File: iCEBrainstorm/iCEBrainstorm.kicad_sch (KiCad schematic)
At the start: 1 part

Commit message: commit from within kicad
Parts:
- added C1, C2, C3, C4, C5: 100nF, PCM_JLCPCB:C_0603, symbol PCM_JLCPCB-Capacitors:0603,100nF
- added C6: 4.7uF, PCM_JLCPCB:C_0805, symbol PCM_JLCPCB-Capacitors:0805,4.7uF
- added C7, C8: 1uF, PCM_JLCPCB:C_0603, symbol PCM_JLCPCB-Capacitors:0603,1uF
- added C9: 10nF, PCM_JLCPCB:C_0603, symbol PCM_JLCPCB-Capacitors:0603,10nF
- added FB1: ~, PCM_JLCPCB:FB_0805, symbol PCM_JLCPCB-Inductors:Ferrite,0805,(2)
- added SW1: BOOT MODE, symbol Switch:SW_SPDT
- added SW2: Tactile Button, 160gf, PCM_JLCPCB:SW_TS-1088-AR02016, symbol PCM_JLCPCB-Connectors_Buttons:Tactile Button, 160gf, 12V, 50mA, 4.0mm
- added U1: STM32F103C8T6, PCM_JLCPCB:LQFP-48_7x7mm_P0.5mm, symbol PCM_JLCPCB-MCUs:STM32F103C8T6
- added U2: CH32V003F4U6, PCM_JLCPCB:QFN-20-1EP_3x3mm_P0.4mm_EP1.65x1.65mm, symbol PCM_JLCPCB-Extended:MCU, CH32V003F4U6
- added U3: ICE40UP5K-SG48ITR, Package_DFN_QFN:QFN-48-1EP_7x7mm_P0.5mm_EP5.6x5.6mm, symbol FPGA_Lattice:ICE40UP5K-SG48ITR
- added X1: X322516MLB4SI, PCM_JLCPCB:OSC-SMD_4P-L3.2-W2.5-BL, symbol PCM_JLCPCB-Crystals:Crystal, 16MHz, 9pF
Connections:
- net at R1.1: now also SW1.2 (B)
- net at R1.2: now also U1.44 (BOOT0)
- new net: U3.30 (VCC), U3.5 (VCC)
- new net: U2.21 (VSS), U2.4 (VSS)
- new net +3.3VA: C8.1, C9.1, FB1.1, U1.9 (VDDA)
- new net +3V3: C2.1, C3.1, C4.1, C5.1, C6.1, C7.1, FB1.2, SW1.1 (A), U1.1 (VBAT), U1.24 (VDD), U1.36 (VDD), U1.48 (VDD)
- new net GND: C1.2, C2.2, C3.2, C4.2, C5.2, C6.2, C7.2, C8.2, C9.2, SW1.3 (C), SW2.2 (B), U1.23 (VSS), U1.35 (VSS), U1.47 (VSS), U1.8 (VSSA)
- new net NRST: C1.1, SW2.1 (A), U1.7 (NRST)
- new net XMIN: U1.6 (PD1), X1.3 (OSC)
- new net XPLUS: U1.5 (PD0), X1.1 (OSC)

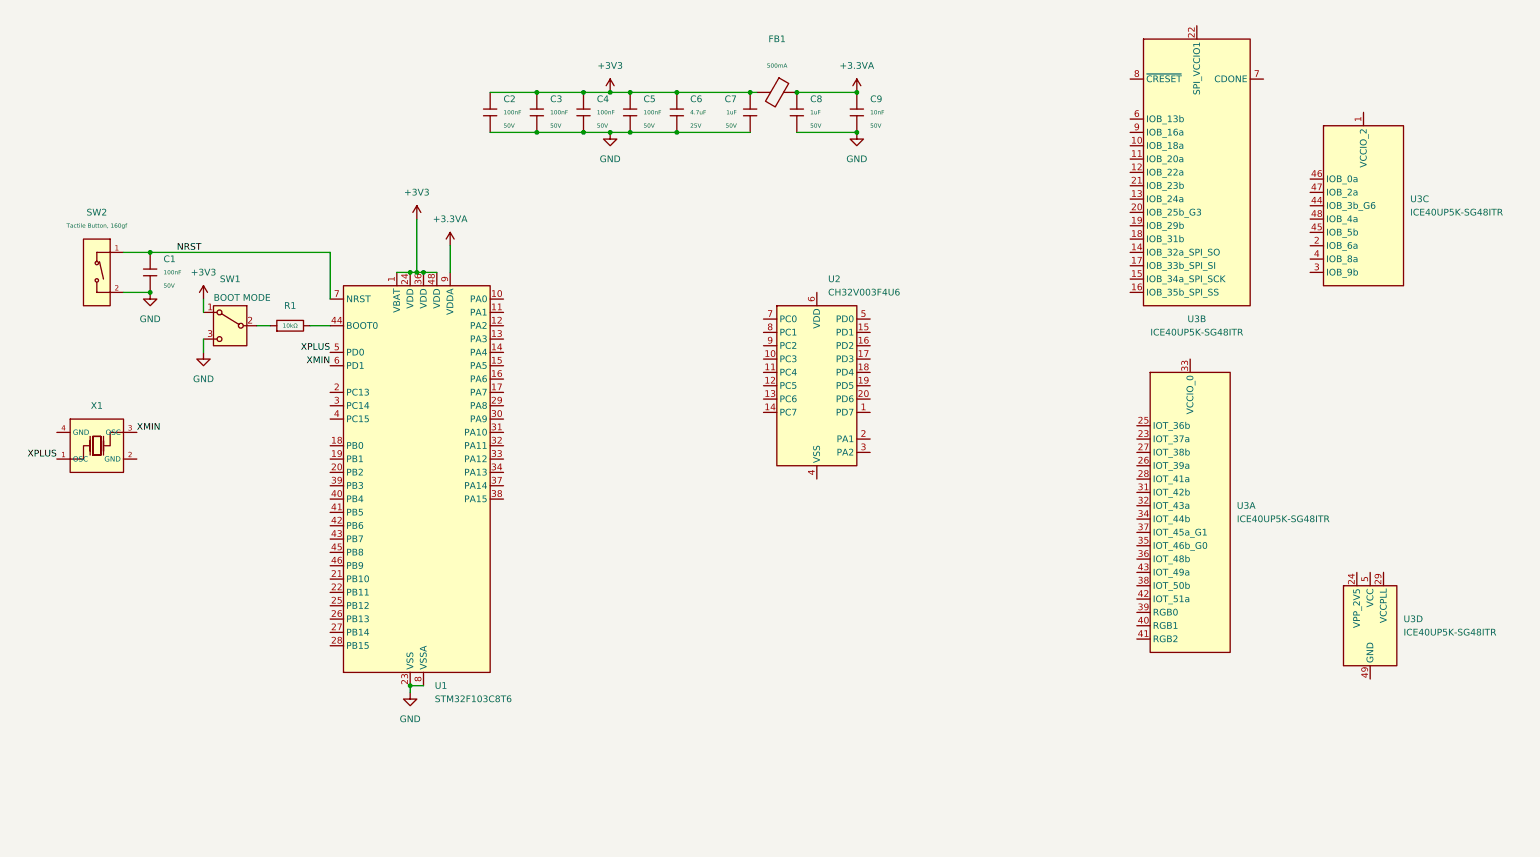
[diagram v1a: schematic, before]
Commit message: added some things to schematic
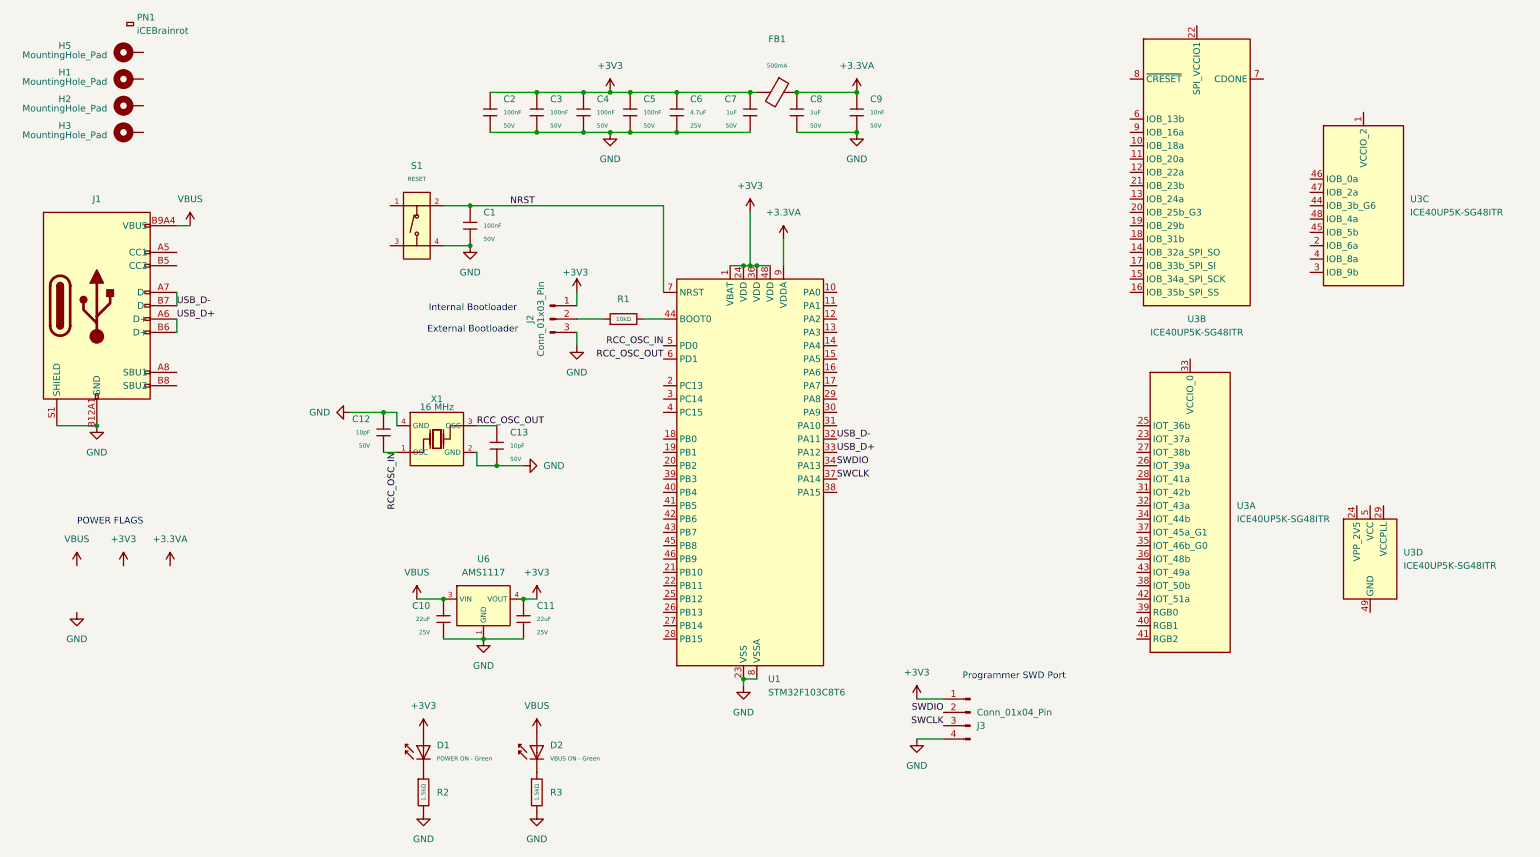
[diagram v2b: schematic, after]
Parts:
- removed SW1: BOOT MODE, symbol Switch:SW_SPDT
- removed SW2: Tactile Button, 160gf, PCM_JLCPCB:SW_TS-1088-AR02016, symbol PCM_JLCPCB-Connectors_Buttons:Tactile Button, 160gf, 12V, 50mA, 4.0mm
- removed U2: CH32V003F4U6, PCM_JLCPCB:QFN-20-1EP_3x3mm_P0.4mm_EP1.65x1.65mm, symbol PCM_JLCPCB-Extended:MCU, CH32V003F4U6
- added C10, C11: 22uF, PCM_JLCPCB:C_0805, symbol PCM_JLCPCB-Capacitors:0805,22uF
- added C12, C13: 10pF, PCM_JLCPCB:C_0603, symbol PCM_JLCPCB-Capacitors:0603,10pF
- added D1: POWER ON - Green, PCM_JLCPCB:D_0805, symbol PCM_JLCPCB-Diodes:LED,0805,Green
- added D2: VBUS ON - Green, PCM_JLCPCB:D_0805, symbol PCM_JLCPCB-Diodes:LED,0805,Green
- added H1, H2, H3: MountingHole_Pad, MountingHole:MountingHole_2.7mm_Pad, symbol Mechanical:MountingHole_Pad
- added H5: MountingHole_Pad, MountingHole:MountingHole_3.2mm_M3_DIN965_Pad, symbol Mechanical:MountingHole_Pad
- added J1: Connector, USB-TYPE-C-16P, PCM_JLCPCB:TYPE-C-SMD_HX-TYPE-C-16PIN, symbol PCM_JLCPCB-Extended:Connector, USB-TYPE-C-16P
- added J2: Conn_01x03_Pin, Connector_PinHeader_2.00mm:PinHeader_1x03_P2.00mm_Vertical, symbol Connector:Conn_01x03_Pin
- added J3: Conn_01x04_Pin, Connector_PinHeader_2.00mm:PinHeader_1x04_P2.00mm_Vertical, symbol Connector:Conn_01x04_Pin
- added PN1: iCEBrainrot, PCM_JLCPCB:Part_Num_JLCPCB, symbol PCM_JLCPCB-Manufacturing:Part Number, PCM_JLCPCB, 0.8x0.15mm
- added R2, R3: 1.5kΩ, PCM_JLCPCB:R_0603, symbol PCM_JLCPCB-Resistors:0603,1.5kΩ
- added S1: RESET, PCM_JLCPCB:SW-SMD_4P-L5.1-W5.1-P3.70-LS6.5-TL-2, symbol PCM_JLCPCB-Connectors_Buttons:Tactile Button, 160gf, 12V, 50mA, 5.1mm
- added U6: AMS1117, PCM_JLCPCB:SOT-223-3_L6.5-W3.4-P2.30-LS7.0-BR, symbol PCM_JLCPCB-Power:LDO, 3.3V, 1A
- X1: value X322516MLB4SI -> 16 MHz
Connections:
- net +3V3: now also C11.2, D1.2, J2.1 (Pin_1), J3.1 (Pin_1), U6.2 (VOUT), U6.4 (VOUT)
- net GND: now also X1.2 (GND), X1.4 (GND), C10.1, C11.1, C12.1, C13.2, J1.A12B1 (GND), J1.B12A1 (GND), J1.S1 (SHIELD), J2.3 (Pin_3), J3.4 (Pin_4), R2.2, R3.2, S1.4 (D), U6.1 (GND)
- net NRST: now also S1.2 (B)
- net at R1.1: now also J2.2 (Pin_2)
- net USB_D-: now reaches U1.32 (PA11)
- net USB_D-: now also J1.A7 (D-), J1.B7 (D-)
- net USB_D+: now reaches U1.33 (PA12)
- net USB_D+: now also J1.A6 (D+), J1.B6 (D+)
- net SWDIO: now reaches U1.34 (PA13)
- net SWDIO: now also J3.2 (Pin_2)
- net SWCLK: now reaches U1.37 (PA14)
- net SWCLK: now also J3.3 (Pin_3)
- net XMIN renamed RCC_OSC_OUT
- net RCC_OSC_OUT: now also C13.1
- net XPLUS renamed RCC_OSC_IN
- net RCC_OSC_IN: now also C12.2
- new net: D1.1, R2.1
- new net: D2.1, R3.1
- new net VBUS: C10.2, D2.2, J1.A9B4 (VBUS), J1.B9A4 (VBUS), U6.3 (VIN)
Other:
- note added: "Internal Bootloader External Bootloader"
- note added: "POWER FLAGS"
- note added: "Programmer SWD Port"
- moved on the sheet: C1, R1, U1, U3D, X1

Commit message: did some things
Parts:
- removed H5: MountingHole_Pad, MountingHole:MountingHole_3.2mm_M3_DIN965_Pad, symbol Mechanical:MountingHole_Pad
- removed J2: Conn_01x03_Pin, Connector_PinHeader_2.00mm:PinHeader_1x03_P2.00mm_Vertical, symbol Connector:Conn_01x03_Pin
- removed R1: 10kΩ, PCM_JLCPCB:R_0603, symbol PCM_JLCPCB-Resistors:0603,10kΩ
- removed U1: STM32F103C8T6, PCM_JLCPCB:LQFP-48_7x7mm_P0.5mm, symbol PCM_JLCPCB-MCUs:STM32F103C8T6
- added C14, C16, C18: 4.7uF, PCM_JLCPCB:C_0805, symbol PCM_JLCPCB-Capacitors:0805,4.7uF
- added C15, C17, C19: 100nF, PCM_JLCPCB:C_0603, symbol PCM_JLCPCB-Capacitors:0603,100nF
- added C20, C21: 22uF, PCM_JLCPCB:C_0805, symbol PCM_JLCPCB-Capacitors:0805,22uF
- added H4: MountingHole_Pad, MountingHole:MountingHole_2.7mm_Pad, symbol Mechanical:MountingHole_Pad
- added R1, R6: 15kΩ, PCM_JLCPCB:R_0603, symbol PCM_JLCPCB-Resistors:0603,15kΩ
- added R4, R5: 5.1kΩ, PCM_JLCPCB:R_0603, symbol PCM_JLCPCB-Resistors:0603,5.1kΩ
- added SW1, SW2: SW_DIP_x08, Button_Switch_THT:SW_DIP_SPSTx08_Slide_6.7x21.88mm_W7.62mm_P2.54mm_LowProfile, symbol Switch:SW_DIP_x08
- added U1: AMS1117-1.2, PCM_JLCPCB:SOT-223-3_L6.5-W3.4-P2.30-LS7.0-BR, symbol PCM_JLCPCB-Power:LDO, 3.3V, 1A
- added U2: STM32F412RETx, Package_QFP:LQFP-64_10x10mm_P0.5mm, symbol MCU_ST_STM32F4:STM32F412RETx
- U6: value AMS1117 -> AMS1117-3.3
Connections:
- net +3.3VA: now also U2.13 (VDDA)
- net +3V3: now also U3.1 (VCCIO_2), U3.22 (SPI_VCCIO1), U3.24 (VPP_2V5), U3.33 (VCCIO_0), C14.1, C15.1, C16.1, C17.1, C18.1, C19.1, SW1.15, SW1.16, U2.1 (VBAT), U2.19 (VDD), U2.32 (VDD), U2.48 (VDD), U2.64 (VDD)
- net GND: now also U3.49 (GND), C14.2, C15.2, C16.2, C17.2, C18.2, C19.2, C20.1, C21.1, R1.2, R4.2, R5.2, R6.2, U1.1 (GND), U2.12 (VSSA), U2.18 (VSS), U2.31 (VSS), U2.47 (VSS), U2.63 (VSS)
- net NRST: now also U2.7 (NRST)
- net VBUS: now also C20.2, U1.3 (VIN)
- net VCCPLL: now reaches U3.29 (VCCPLL)
- net +1V2: now reaches U3.30 (VCC), U3.5 (VCC)
- net +1V2: now also C21.2, U1.2 (VOUT), U1.4 (VOUT)
- net at U3.25 (IOT_36b): now also U2.14 (PA0)
- net at J1.A5 (CC1): now also R4.1
- net at J1.B5 (CC2): now also R5.1
- new net BOOT0: R1.1, SW1.1, U2.60 (BOOT0)
- new net BOOT1: R6.1, SW1.2, U2.28 (PB2)
- no-connect marks 0 -> 2
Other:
- note added: "5k1 Resistor like in this Tutorial"
- note added: "SW1 OFF: Custom Boot SW1 ON: STM Bootloader SW2 OFF: System Memory (default) SW2 ON: Embedded SRAM Boot"
- note added: "note: this is not 100% correct, as there should be a 10K between 3V3 and the BOOT pin"
- note added: "note: this might better be 2V5"
- note removed: "Internal Bootloader External Bootloader"
- moved on the sheet: C10, C11, H1, H2, H3, J3, U3A, U3B, U3C, U3D, U6

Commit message: schema und pcb gmacht, quote kostet jetzt 120$ / 10 pcs
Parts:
- removed J3: Conn_01x04_Pin, Connector_PinHeader_2.00mm:PinHeader_1x04_P2.00mm_Vertical, symbol Connector:Conn_01x04_Pin
- added C1, C10, C17, C28, C3: 100nF, PCM_JLCPCB:C_0603, symbol PCM_JLCPCB-Capacitors:0603,100nF
- added C2, C6: 4.7uF, PCM_JLCPCB:C_0805, symbol PCM_JLCPCB-Capacitors:0805,4.7uF
- added D1: M4, PCM_JLCPCB:D_SMA, symbol PCM_JLCPCB-Diodes:General,M4
- added D2: 1V2 ON - Green, PCM_JLCPCB:D_0805, symbol PCM_JLCPCB-Diodes:LED,0805,Green
- added D5: Configuration Ready - Green, PCM_JLCPCB:D_0805, symbol PCM_JLCPCB-Diodes:LED,0805,Green
- added J2: Conn_01x06_Pin, Connector_PinHeader_1.27mm:PinHeader_1x06_P1.27mm_Vertical, symbol Connector:Conn_01x06_Pin
- added J3: Connector, USB-TYPE-C-16P, PCM_JLCPCB:TYPE-C-SMD_HX-TYPE-C-16PIN, symbol PCM_JLCPCB-Extended:Connector, USB-TYPE-C-16P
- added Q1: HL2312, PCM_JLCPCB:Q_SOT-23, symbol PCM_JLCPCB-Transistors:NMOS,HL2312
- added R12, R19, R20, R8: 15kΩ, PCM_JLCPCB:R_0603, symbol PCM_JLCPCB-Resistors:0603,15kΩ
- added R14, R15: 5.1kΩ, PCM_JLCPCB:R_0603, symbol PCM_JLCPCB-Resistors:0603,5.1kΩ
- added R16, R6, R7, R9: 1.5kΩ, PCM_JLCPCB:R_0603, symbol PCM_JLCPCB-Resistors:0603,1.5kΩ
- added R17, R18: 68Ω, PCM_JLCPCB:R_0603, symbol PCM_JLCPCB-Resistors:0603,68Ω
- added R21: 2.2kΩ, PCM_JLCPCB:R_0603, symbol PCM_JLCPCB-Resistors:0603,2.2kΩ
- added R5: 100Ω, PCM_JLCPCB:R_0603, symbol PCM_JLCPCB-Resistors:0603,100Ω
- added S1: RESET, PCM_JLCPCB:SW-SMD_4P-L5.1-W5.1-P3.70-LS6.5-TL-2, symbol PCM_JLCPCB-Connectors_Buttons:Tactile Button, 160gf, 12V, 50mA, 5.1mm
- added U5: W25Q128, PCM_JLCPCB:SOIC-8_L5.3-W5.3-P1.27-LS8.0-BL, symbol PCM_JLCPCB-Memory:16MByte, SPI
- D3: renamed from D1; value POWER ON - Green -> 3V3 ON - Green
- renumbered C1 to C11, C2 to C12, C3 to C14, C4 to C15, C5 to C16, C6 to C18, C7 to C19, C8 to C20, C9 to C21, C14 to C22, C15 to C23, C16 to C24, C17 to C25, C18 to C26, C19 to C27, C10 to C4, C20 to C5, C11 to C7, C21 to C8, C12 to C9, D2 to D4, R2 to R10, R3 to R11, R6 to R2, R4 to R3, R5 to R4, S1 to S2, U6 to U1, U1 to U2, U2 to U3, U3 to U4
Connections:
- net RCC_OSC_IN is gone; now on net OSC_IN: C9.2, X1.1 (OSC)
- net RCC_OSC_OUT is gone; now on net OSC_OUT: C13.1, X1.3 (OSC)
- net USB_D+ is gone; now on net USB_DP: J1.A6 (D+), J1.B6 (D+)
- net USB_D- is gone; now on net USB_DN: J1.A7 (D-), J1.B7 (D-)
- net +1V2: now also Q1.1 (G), R5.2, R8.1
- net +3V3: now also C1.1, C28.1, D1.2, J2.1 (Pin_1), R12.1, R19.1, R20.1, R21.1, R6.2, R7.2, U5.8 (VCC); no longer SW1.15, SW1.16, U4.24 (VPP_2V5)
- net GND: now also C1.2, C10.2, C17.1, C2.2, C28.2, C3.2, C6.2, D5.1, J2.6 (Pin_6), J3.A12B1 (GND), J3.B12A1 (GND), J3.S1 (SHIELD), Q1.2 (S), R14.2, R15.2, R8.2, S1.4 (D), U5.4 (GND)
- net NRST: now also J2.5 (Pin_5)
- net SWCLK: now also U3.49 (PA14), J2.2 (Pin_2)
- net SWDIO: now also U3.46 (PA13), J2.3 (Pin_3)
- net VBUS: now also D2.2, J3.A9B4 (VBUS), J3.B9A4 (VBUS)
- net VCCPLL: now also C3.1, C6.1, R5.1
- net SPI2_SCK: now reaches U4.10 (IOB_18a)
- net SPI2_SCK: now also U3.34 (PB13)
- net SPI2_NSS: now reaches U4.11 (IOB_20a)
- net SPI2_NSS: now also U3.33 (PB12)
- net at U4.12 (IOB_22a): now also R16.1
- net at U4.13 (IOB_24a): now also R18.2
- net FPGA_SPI_SO: now reaches U4.14 (IOB_32a_SPI_SO)
- net FPGA_SPI_SO: now also U5.5 (DI)
- net FPGA_SPI_SCK: now reaches U4.15 (IOB_34a_SPI_SCK)
- net FPGA_SPI_SCK: now also U5.6 (CLK)
- net FPGA_SPI_CS: now reaches U4.16 (IOB_35b_SPI_SS)
- net FPGA_SPI_CS: now also U5.1 (CS#)
- net FPGA_SPI_SI: now reaches U4.17 (IOB_33b_SPI_SI)
- net FPGA_SPI_SI: now also U5.2 (DO)
- net FPGA_CLK: now reaches U4.20 (IOB_25b_G3)
- net FPGA_CLK: now also U3.40 (PC9)
- net at U4.21 (IOB_23b): now also R17.2
- net SPI2_MOSI: now reaches U4.6 (IOB_13b)
- net SPI2_MOSI: now also U3.36 (PB15)
- net at U4.7 (CDONE): now also D5.2, R21.2
- net FPGA_NRST: now reaches U4.8 (~{CRESET})
- net FPGA_NRST: now also C10.1, R12.2, S1.2 (B)
- net SPI2_MISO: now reaches U4.9 (IOB_16a)
- net SPI2_MISO: now also U3.35 (PB14)
- net at U3.14 (PA0): no longer U4.25 (IOT_36b)
- net at U3.30 (VCAP_1): now also C17.2
- net USB_SOF: now reaches U3.41 (PA8)
- net USB_VBUS: now reaches U3.42 (PA9)
- net USB_ID: now reaches U3.43 (PA10)
- net USB_DN: now reaches U3.44 (PA11)
- net USB_DP: now reaches U3.45 (PA12)
- net OSC_IN: now reaches U3.5 (PH0)
- net SWO: now reaches U3.55 (PB3)
- net OSC_OUT: now reaches U3.6 (PH1)
- new net: J3.A5 (CC1), R14.1
- new net: R19.2, U5.3 (IO2)
- new net: R20.2, U5.7 (IO3)
- new net: R7.1, SW1.15
- new net: R6.1, SW1.16
- new net: J3.B5 (CC2), R15.1
- new net: D2.1, R9.1
- new net: Q1.3 (D), R9.2
- new net +2V5: C2.1, D1.1, U4.24 (VPP_2V5)
- new net FPGA_USB_DN: J3.A7 (D-), J3.B7 (D-), R16.2, R17.1
- new net FPGA_USB_DP: J3.A6 (D+), J3.B6 (D+), R18.1
- new net SWDO: J2.4 (Pin_4)
- no-connect marks 2 -> 8
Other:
- note added: "POWER GENERATION"
- note added: "STATUS LED'S"
- note added: "STM USB"
- note added: "misc"
- note added: "using the RCC MCO to output the Clock through this pin"
- note removed: "note: this might better be 2V5"
- moved on the sheet: C11, C12, C13, C14, C15, C16, C18, C19, C20, C21, C22, C23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

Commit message: pascuu design review
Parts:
- removed D1: M4, PCM_JLCPCB:D_SMA, symbol PCM_JLCPCB-Diodes:General,M4
- added J5: Conn_01x06_Pin, Connector_PinHeader_1.27mm:PinHeader_1x06_P1.27mm_Vertical, symbol Connector:Conn_01x06_Pin
- added JP1: SolderJumper_2_Bridged, Jumper:SolderJumper-2_P1.3mm_Bridged_RoundedPad1.0x1.5mm, symbol Jumper:SolderJumper_2_Bridged
- added JP2, JP3, JP4, JP5: SolderJumper_2_Bridged, symbol Jumper:SolderJumper_2_Bridged
- added JP6, JP7, JP8, JP9: SolderJumper_2_Open, symbol Jumper:SolderJumper_2_Open
- added R13, R23: 1.5kΩ, PCM_JLCPCB:R_0603, symbol PCM_JLCPCB-Resistors:0603,1.5kΩ
- added R22: 15kΩ, PCM_JLCPCB:R_0603, symbol PCM_JLCPCB-Resistors:0603,15kΩ
- C10: now not fitted
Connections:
- net +2V5: now also C1.1, JP1.2 (B)
- net +3V3: now also J5.1 (Pin_1), JP1.1 (A), R22.1; no longer C1.1
- net BOOT1: now also R2.2; no longer R2.1
- net FPGA_SPI_CS: now also SW1.4, J5.2 (Pin_2), JP5.1 (A), JP6.2 (B); no longer U4.16 (IOB_35b_SPI_SS)
- net FPGA_SPI_SCK: now also J5.5 (Pin_5), JP4.1 (A), JP7.2 (B); no longer U4.15 (IOB_34a_SPI_SCK)
- net FPGA_SPI_SI: now also J5.3 (Pin_3), JP3.1 (A), JP9.2 (B); no longer U4.17 (IOB_33b_SPI_SI)
- net FPGA_SPI_SO: now also J5.4 (Pin_4), JP2.1 (A), JP8.2 (B); no longer U4.14 (IOB_32a_SPI_SO)
- net GND: now also R2.1, J5.6 (Pin_6), R13.2, R23.2; no longer R2.2
- net SPI2_MISO: now also U4.31 (IOT_42b); no longer U4.9 (IOB_16a)
- net SPI2_MOSI: now also U4.28 (IOT_41a); no longer U4.6 (IOB_13b)
- net SPI2_NSS: now also U4.34 (IOT_44b); no longer U4.11 (IOB_20a)
- net SPI2_SCK: now also U4.32 (IOT_43a); no longer U4.10 (IOB_18a)
- net at SW1.13: now also R23.1
- net at SW1.14: now also R13.1
- net FPGA_BOOT: now reaches SW1.3
- net FPGA_BOOT: now also U4.9 (IOB_16a), R22.2
- net FPGA_GLOBAL_6: now reaches U4.44 (IOB_3b_G6)
- net at U3.20 (PA4): now also JP6.1 (A)
- net at U3.21 (PA5): now also JP7.1 (A)
- net at U3.22 (PA6): now also JP8.1 (A)
- net at U3.23 (PA7): now also JP9.1 (A)
- net FPGA_GLOBAL_0: now reaches U3.29 (PB10)
- net FPGA_GLOBAL_0: now also U4.35 (IOT_46b_G0)
- net FPGA_GLOBAL_1: now reaches U4.37 (IOT_45a_G1)
- net FPGA_USB_DN renamed FPGA_USB_D+
- net FPGA_USB_D+: now also J3.A6 (D+), J3.B6 (D+); no longer J3.A7 (D-), J3.B7 (D-)
- removed net FPGA_USB_DP: J3.A6 (D+), J3.B6 (D+), R18.1
- net USB_DN renamed USB_D-
- net USB_DP renamed USB_D+
- new net: JP5.2 (B), U4.16 (IOB_35b_SPI_SS)
- new net: JP4.2 (B), U4.15 (IOB_34a_SPI_SCK)
- new net: JP2.2 (B), U4.14 (IOB_32a_SPI_SO)
- new net: JP3.2 (B), U4.17 (IOB_33b_SPI_SI)
- new net FPGA_USB_D-: J3.A7 (D-), J3.B7 (D-), R18.1
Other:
- note added: "SW1 OFF: Custom Boot SW1 ON: STM Bootloader SW2 OFF: System Memory (default) SW2 ON: Embedded SRAM Boot SW3 OFF: FPGA Custom Boot SW3 ON: FPGA USB DFU Programmer SW4 OFF: FPGA Boot from Flash SW4 ON: FPGA Boot from SPI"
- note added: "TODO: is this correct? D+ or D- ??"
- note added: "acces to FPGA flash"
- note removed: "SW1 OFF: Custom Boot SW1 ON: STM Bootloader SW2 OFF: System Memory (default) SW2 ON: Embedded SRAM Boot"
- moved on the sheet: C1, R1, R18, R2
